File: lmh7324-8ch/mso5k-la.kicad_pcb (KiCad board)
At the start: 4 copper layers, 40 x 44 mm, 101 parts, among them IC201 lmh7324, IC401 lmh7324, J101 out, J102 in, J103 3mm, J104 3mm, J105 3mm, J106 3mm, U401 ATtiny85-20SU

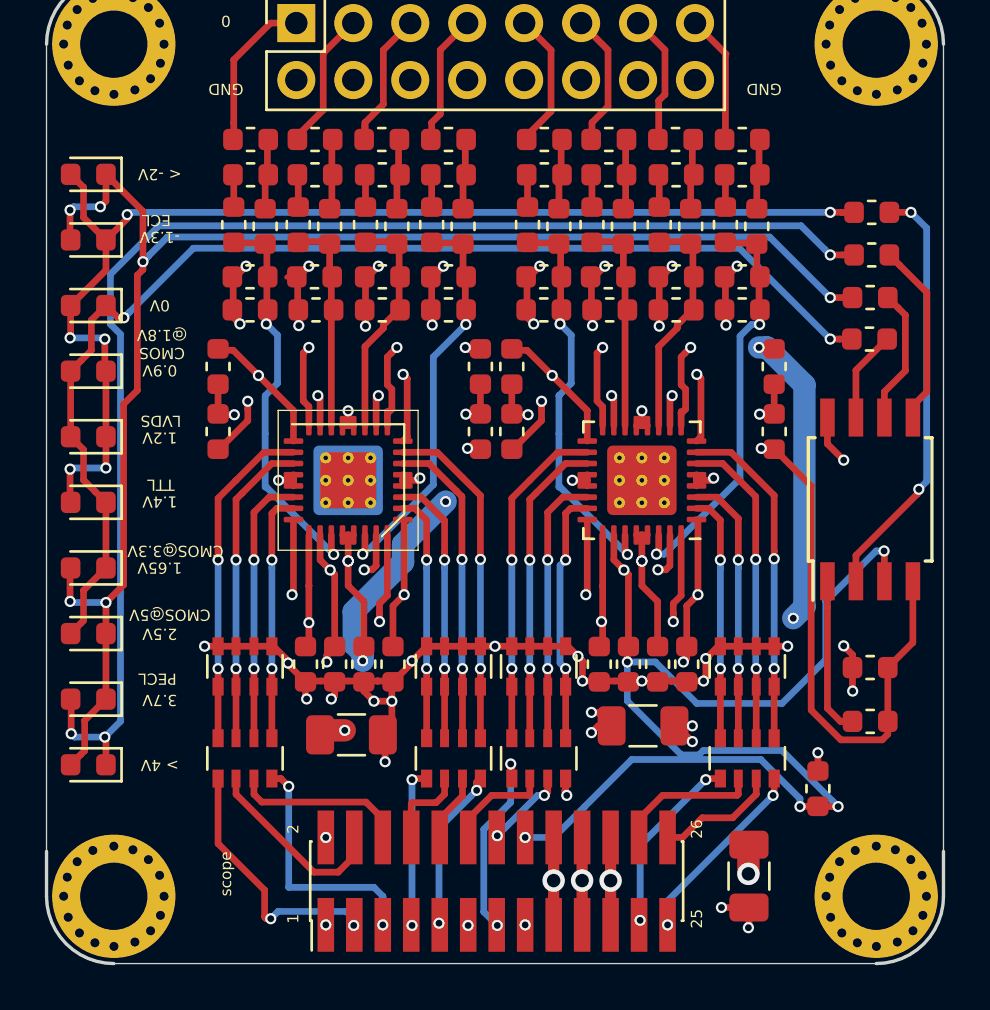
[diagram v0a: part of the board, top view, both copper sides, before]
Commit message: Added breakout
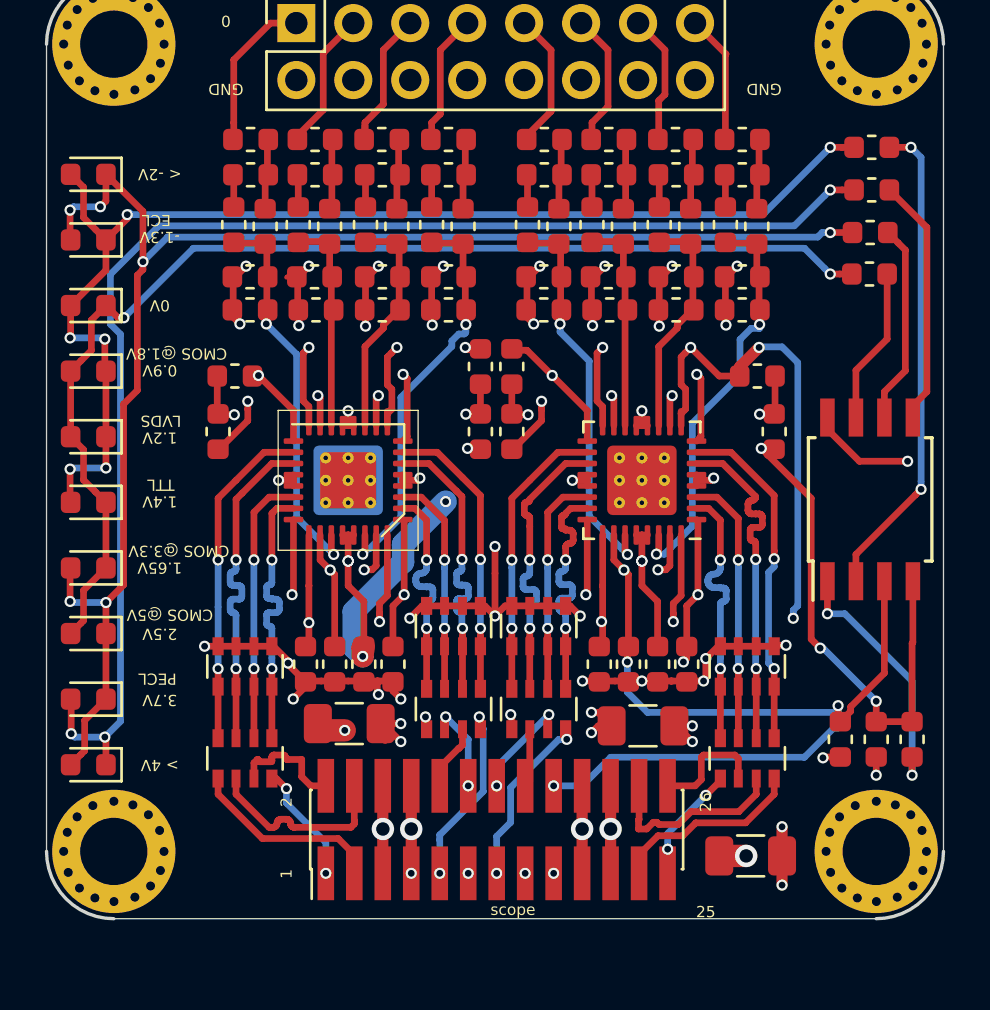
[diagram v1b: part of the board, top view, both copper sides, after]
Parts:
- moved C417 3.21 mm to (82.0, 179.0), turned to 90 degrees
- moved R418 2.90 mm to (81.8, 154.5)
- moved R419 2.90 mm to (81.7, 156.4)
- moved R420 2.90 mm to (81.7, 158.2)
- moved R421 2.90 mm to (81.8, 152.6)
- moved C104 2.42 mm to (80.4, 179.0), turned to 270 degrees
- moved J101 2.30 mm to (65.1, 183.0)
- moved RN202 2.20 mm to (67.0, 177.7)
- moved RN404 2.20 mm to (63.1, 177.7)
- moved R417 2.03 mm to (83.6, 179.0), turned to 90 degrees
- moved J104 2.00 mm to (48.0, 184.0)
- moved J106 2.00 mm to (82.0, 184.0)
- moved RN201 1.80 mm to (67.0, 173.9)
- moved RN403 1.80 mm to (63.1, 173.9)
- moved C102 0.90 mm to (76.4, 184.2), turned to 0 degrees
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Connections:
- J101 pad 1: GND -> D0-
- J101 pad 11: D4- -> D3-
- J101 pad 12: D5+ -> D3+
- J101 pad 13: D5- -> D4-
- J101 pad 15: GND -> D5-
- J101 pad 16: Vref -> D5+
- J101 pad 17: -2V5 -> GND
- J101 pad 18: -2V5 -> Vref
- J101 pad 2: GND -> D0+
- J101 pad 23: D7- -> D6-
- J101 pad 24: D7+ -> D6+
- J101 pad 25: D6- -> D7-
- J101 pad 26: D6+ -> D7+
- J101 pad 5: D0- -> -2V5
- J101 pad 6: D0+ -> -2V5
- J101 pad 7: D3- -> GND
- J101 pad 8: D3+ -> GND
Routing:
- net GND: track 272.3 -> 233.2 mm, vias 43 -> 44
- net Vref: track 144.4 -> 129.9 mm, vias 16 -> 13
- net -2V5: track 127.7 -> 113.6 mm, vias 16 -> 18
- net +2V5: track 155.2 -> 167.3 mm, vias 14 -> 13
- net +4V: track 108.2 -> 100.1 mm
- net D0-: track 12.3 -> 5.41 mm
- net Net-(R417-Pad1): track 7.03 -> 11.5 mm, vias 0 -> 2
- net D7-: track 8.38 -> 5.20 mm
- net D6+: track 5.45 -> 8.61 mm
- net Net-(R420-Pad2): track 4.08 -> 6.98 mm
- net Net-(R419-Pad2): track 6.06 -> 8.96 mm
- net Net-(R418-Pad2): track 8.20 -> 11.1 mm
- net D1-: track 11.9 -> 9.01 mm, vias 2 -> 0
- net Net-(R421-Pad2): track 19.0 -> 21.7 mm
- net D0+: track 7.73 -> 5.31 mm
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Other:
- board size 40 x 44 mm -> 40 x 42 mm
- board text added: "CMOS @3.3V"
- board text added: "CMOS @5V"
- board text removed: "CMOS@3.3V"
- board text removed: "CMOS@5V"

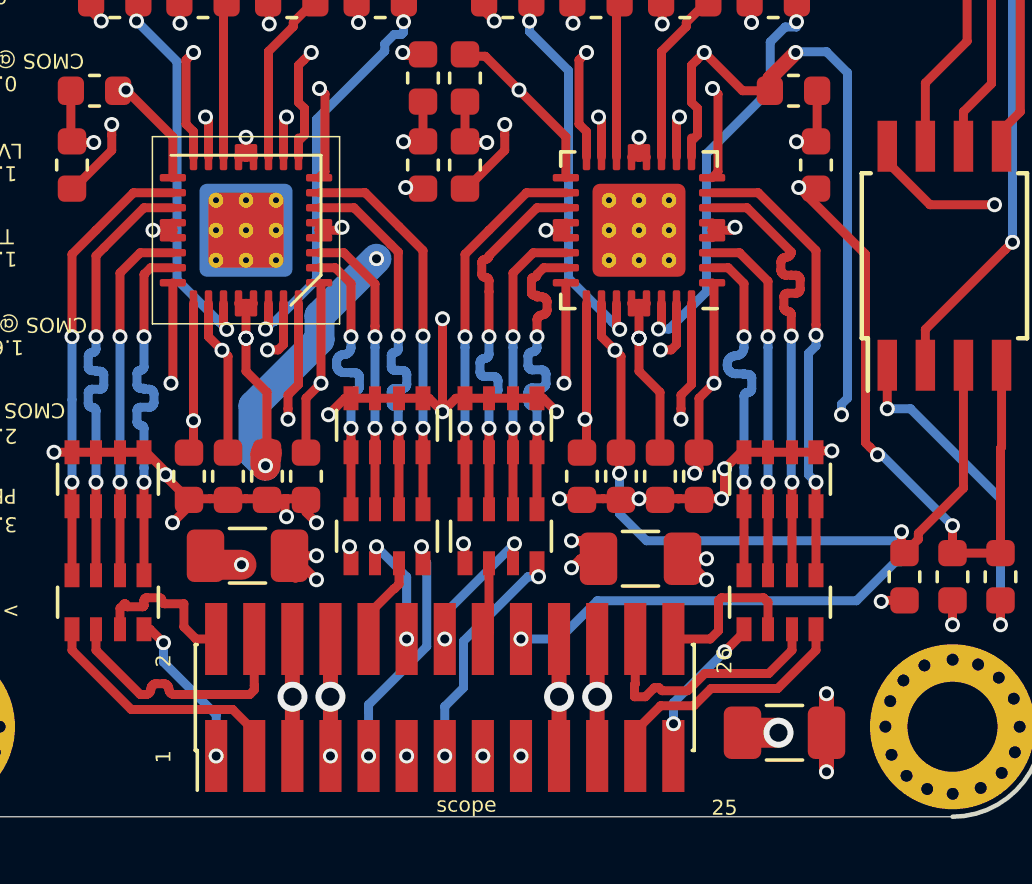
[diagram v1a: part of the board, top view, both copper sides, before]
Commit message: Switched to 0805 on the pod for the large bulk caps
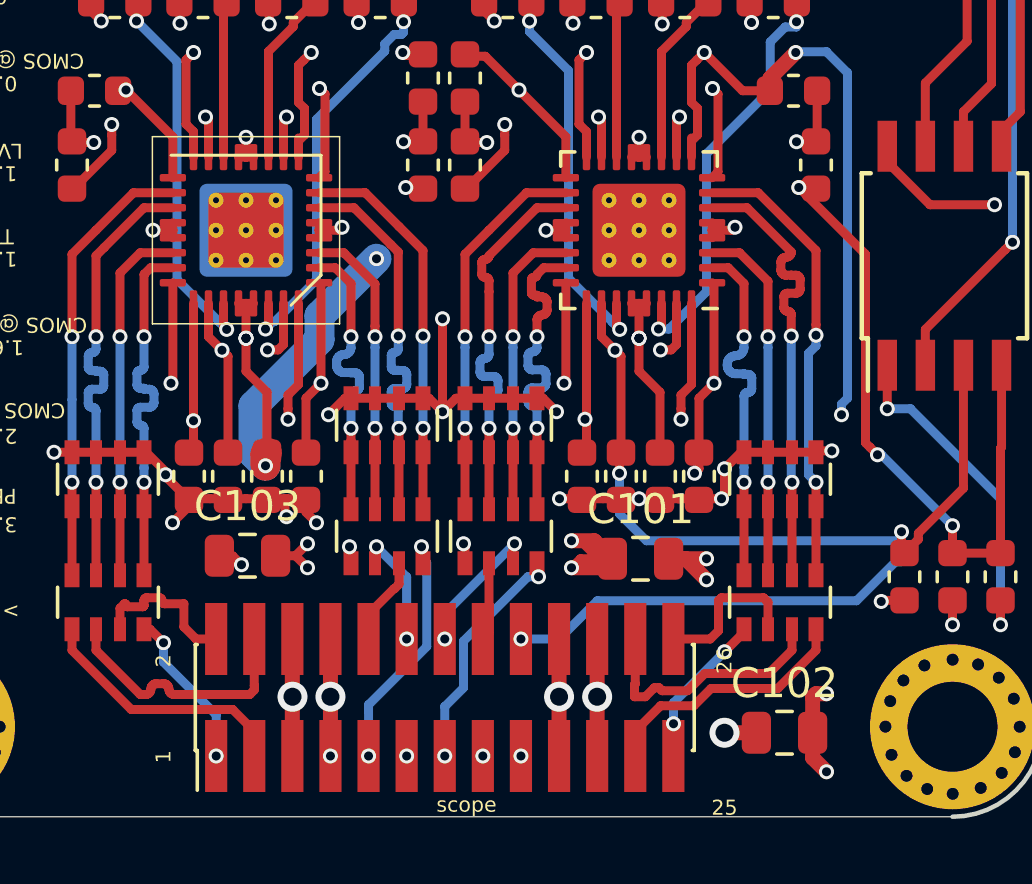
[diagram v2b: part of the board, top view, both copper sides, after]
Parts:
- added G***: LOGO, lmh7324-8ch:qrcode, B.Cu at (65.2, 157.7)
- C101, C102, C103: footprint Capacitor_SMD:C_1206_3216Metric -> Capacitor_SMD:C_0805_2012Metric
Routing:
- net +2V5: track 167.3 -> 163.8 mm
- net +4V: track 100.1 -> 103.2 mm
- net GND: track 233.2 -> 235.0 mm
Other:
- board text added: "MSO5k LMH7324 8 channel LA pod https://dren.dk https://gitlab.com/dren.dk/mso5k-la-pod 2019-01-30"

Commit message: Added proper readme
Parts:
- added C217: 10n, Capacitor_SMD:C_0402_1005Metric, B.Cu at (32.1, 35.6)
- added C218: 10n, Capacitor_SMD:C_0402_1005Metric, B.Cu at (28.6, 39.2)
- added C219: 10n, Capacitor_SMD:C_0402_1005Metric, B.Cu at (29.7, 35.7)
- added C220: 10n, Capacitor_SMD:C_0402_1005Metric, B.Cu at (33.3, 39.3)
- added C221: 10n, Capacitor_SMD:C_0402_1005Metric, B.Cu at (29.6, 40.1)
- added C222: 10n, Capacitor_SMD:C_0402_1005Metric, B.Cu at (33.1, 36.6)
- added C223: 10n, Capacitor_SMD:C_0402_1005Metric, B.Cu at (32.2, 40.1)
- added C224: 10n, Capacitor_SMD:C_0402_1005Metric, B.Cu at (28.7, 36.7)
- added C225: 10n, Capacitor_SMD:C_0402_1005Metric, B.Cu at (33.0, 38.0)
- added C226: 10n, Capacitor_SMD:C_0402_1005Metric, B.Cu at (30.9, 40.0)
- added C227: 10n, Capacitor_SMD:C_0402_1005Metric, B.Cu at (30.9, 35.9)
- added C228: 10n, Capacitor_SMD:C_0402_1005Metric, B.Cu at (28.9, 38.0)
- added C301: 10n, Capacitor_SMD:C_0402_1005Metric, B.Cu at (45.4, 40.0)
- added C302: 10n, Capacitor_SMD:C_0402_1005Metric, B.Cu at (41.7, 36.6)
- added C303: 10n, Capacitor_SMD:C_0402_1005Metric, B.Cu at (42.7, 35.7)
- added C304: 10n, Capacitor_SMD:C_0402_1005Metric, B.Cu at (46.5, 36.6)
- added C305: 10n, Capacitor_SMD:C_0402_1005Metric, B.Cu at (42.7, 40.1)
- added C306: 10n, Capacitor_SMD:C_0402_1005Metric, B.Cu at (41.7, 39.2)
- added C307: 10n, Capacitor_SMD:C_0402_1005Metric, B.Cu at (45.3, 35.7)
- added C308: 10n, Capacitor_SMD:C_0402_1005Metric, B.Cu at (46.5, 39.2)
- added C309: 10n, Capacitor_SMD:C_0402_1005Metric, B.Cu at (46.1, 38.0)
- added C310: 10n, Capacitor_SMD:C_0402_1005Metric, B.Cu at (44.0, 35.9)
- added C311: 10n, Capacitor_SMD:C_0402_1005Metric, B.Cu at (42.0, 38.0)
- added C312: 10n, Capacitor_SMD:C_0402_1005Metric, B.Cu at (44.0, 40.0)
- moved RN402 134.6 mm to (26.3, 48.1)
- moved RN204 134.6 mm to (48.8, 48.1)
- moved RN401 134.2 mm to (26.3, 44.4)
- moved RN203 134.2 mm to (48.8, 44.4)
- moved C101 132.4 mm to (44.1, 48.9)
- moved C102 132.4 mm to (48.9, 54.7)
- moved C103 132.4 mm to (31.0, 48.8)
- moved C104 132.4 mm to (52.9, 49.5)
- moved C201 132.4 mm to (39.0, 26.6)
- moved C202 132.4 mm to (41.8, 26.6)
- moved C203 132.4 mm to (39.7, 30.4)
- moved C204 132.4 mm to (42.6, 30.4)
- moved C205 132.4 mm to (43.5, 46.1)
- moved C206 132.4 mm to (38.2, 35.8)
- moved C207 132.4 mm to (42.1, 46.1)
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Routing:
- net GND: track 235.0 -> 252.5 mm, vias 44 -> 48
- net +4V: track 103.2 -> 86.4 mm, vias 14 -> 19
- net +2V5: track 163.8 -> 155.6 mm, vias 13 -> 22
- net D2+: track 2.96 -> 8.95 mm, vias 0 -> 2
- net D5+: track 2.61 -> 7.98 mm, vias 0 -> 2
- net D0+: track 5.31 -> 10.5 mm, vias 0 -> 2
- net D7+: track 5.27 -> 10.1 mm
- net D3+: track 4.06 -> 8.66 mm
- net -2V5: track 113.7 -> 118.2 mm, vias 18 -> 16
- net D4+: track 4.81 -> 9.00 mm
- net D6-: track 8.67 -> 11.8 mm, vias 0 -> 2
- net D1-: track 9.01 -> 12.0 mm
- net D0-: track 5.41 -> 8.22 mm
- net D7-: track 5.20 -> 7.98 mm, vias 2 -> 0
- net /Ch 0-3/A-: track 12.2 -> 9.59 mm, vias 2 -> 0
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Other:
- board text added: "MSO5k LMH7324 8 channel LA pod https://dren.dk https://gitlab.com/dren.dk/mso5k-la-pod 2019-02-14"
- board text removed: "MSO5k LMH7324 8 channel LA pod https://dren.dk https://gitlab.com/dren.dk/mso5k-la-pod 2019-01-30"

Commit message: Added fixes for E1 and E2
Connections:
- D407 pad 2: Net-(D403-Pad2) -> Net-(D401-Pad1)
- D408 pad 1: Net-(D403-Pad2) -> Net-(D401-Pad1)
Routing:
- net Net-(D401-Pad1): track 60.2 -> 65.5 mm, vias 3 -> 4
- net Net-(D403-Pad2): track 51.8 -> 53.2 mm
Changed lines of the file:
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@@
     (thickness 1.6)
     (drawings 34)
-    (tracks 1692)
+    (tracks 1699)
     (zones 0)
     (modules 126)
@@
     (fp_line (start 0.8 -0.4) (end -0.5 -0.4) (layer F.Fab) (width 0.1))
     (pad 2 smd roundrect (at 0.7875 0 180) (size 0.875 0.95) (layers F.Cu F.Paste F.Mask) (roundrect_rratio 0.25)
-      (net 72 "Net-(D403-Pad2)"))
+      (net 71 "Net-(D401-Pad1)"))
     (pad 1 smd roundrect (at -0.7875 0 180) (size 0.875 0.95) (layers F.Cu F.Paste F.Mask) (roundrect_rratio 0.25)
       (net 73 "Net-(D405-Pad2)"))
@@
     )
     (pad 1 smd roundrect (at -0.7875 0 180) (size 0.875 0.95) (layers F.Cu F.Paste F.Mask) (roundrect_rratio 0.25)
-      (net 72 "Net-(D403-Pad2)"))
+      (net 71 "Net-(D401-Pad1)"))
     (pad 2 smd roundrect (at 0.7875 0 180) (size 0.875 0.95) (layers F.Cu F.Paste F.Mask) (roundrect_rratio 0.25)
       (net 73 "Net-(D405-Pad2)"))
@@
   (segment (start 33.125 32.025) (end 36.175 32.025) (width 1) (layer 3_Misc) (net 1))
   (segment (start 36.175 32.025) (end 37.575 32.025) (width 1) (layer 3_Misc) (net 1))
-  (via (at 41.8 48.3) (size 0.5) (drill 0.3) (layers F.Cu B.Cu) (net 1) (status 1000000))
+  (via (at 41.8 48.3) (size 0.5) (drill 0.3) (layers F.Cu B.Cu) (net 1))
   (via (at 42.655 53.5) (size 1) (drill 0.6) (layers F.Cu B.Cu) (net 1))
   (segment (start 41.8 48.3) (end 42.1 48.3) (width 0.3) (layer F.Cu) (net 1) (status 20))
@@
   (segment (start 18.55 41.881928) (end 18.574213 41.857715) (width 0.3) (layer F.Cu) (net 70) (status 30))
   (segment (start 18.55 43.35) (end 18.55 41.881928) (width 0.3) (layer F.Cu) (net 70) (status 20))
-  (segment (start 20.15 43.4) (end 20.936723 42.613277) (width 0.3) (layer F.Cu) (net 70))
   (segment (start 18.7 25.75) (end 18.55 25.9) (width 0.3) (layer B.Cu) (net 70))
   (segment (start 19.9 25.75) (end 18.7 25.75) (width 0.3) (layer B.Cu) (net 70))
   (via (at 21.8 28.2) (size 0.5) (drill 0.3) (layers F.Cu B.Cu) (net 70))
-  (segment (start 21.8 28.553553) (end 21.55 28.803553) (width 0.3) (layer F.Cu) (net 70))
-  (segment (start 21.8 28.2) (end 21.8 28.553553) (width 0.3) (layer F.Cu) (net 70))
-  (segment (start 21.55 33.936723) (end 20.936723 34.55) (width 0.3) (layer F.Cu) (net 70))
-  (segment (start 21.55 28.803553) (end 21.55 33.936723) (width 0.3) (layer F.Cu) (net 70))
-  (segment (start 20.936723 42.613277) (end 20.936723 34.55) (width 0.3) (layer F.Cu) (net 70))
   (segment (start 21.8 25.954968) (end 20.149213 24.304181) (width 0.3) (layer F.Cu) (net 70) (status 20))
   (segment (start 21.8 28.2) (end 21.8 25.954968) (width 0.3) (layer F.Cu) (net 70))
@@
   (segment (start 21.8 28.2) (end 22.898227 27.101773) (width 0.3) (layer B.Cu) (net 70))
   (segment (start 22.898227 27.101773) (end 51.894674 27.101773) (width 0.3) (layer B.Cu) (net 70))
+  (segment (start 22.090002 41.459998) (end 22.090002 28.490002) (width 0.3) (layer F.Cu) (net 70))
+  (segment (start 20.15 43.4) (end 22.090002 41.459998) (width 0.3) (layer F.Cu) (net 70))
+  (segment (start 22.049999 28.449999) (end 21.8 28.2) (width 0.3) (layer F.Cu) (net 70))
+  (segment (start 22.090002 28.490002) (end 22.049999 28.449999) (width 0.3) (layer F.Cu) (net 70))
   (segment (start 53.5125 25) (end 52.975 25) (width 0.3) (layer F.Cu) (net 71) (status 10))
   (via (at 52.45 25) (size 0.5) (drill 0.3) (layers F.Cu B.Cu) (net 71))
@@
   (segment (start 22.510234 26.601762) (end 50.848238 26.601762) (width 0.3) (layer B.Cu) (net 71))
   (segment (start 20.799989 48.700011) (end 20.799989 31.438001) (width 0.3) (layer B.Cu) (net 71))
-  (segment (start 20.349989 30.988001) (end 20.349989 28.762007) (width 0.3) (layer B.Cu) (net 71))
   (segment (start 20.799989 31.438001) (end 20.349989 30.988001) (width 0.3) (layer B.Cu) (net 71))
   (segment (start 20.1 49.4) (end 20.799989 48.700011) (width 0.3) (layer B.Cu) (net 71))
+  (segment (start 19.035825 32.619336) (end 19.035825 32.194175) (width 0.3) (layer F.Cu) (net 71))
+  (segment (start 18.574213 33.080948) (end 19.035825 32.619336) (width 0.3) (layer F.Cu) (net 71))
+  (segment (start 19.035825 32.194175) (end 19.4 31.83) (width 0.3) (layer F.Cu) (net 71))
+  (segment (start 19.4 30.904572) (end 20.149213 30.155359) (width 0.3) (layer F.Cu) (net 71))
+  (segment (start 19.4 31.83) (end 19.4 30.904572) (width 0.3) (layer F.Cu) (net 71))
+  (via (at 20.72 29.05) (size 0.5) (drill 0.3) (layers F.Cu B.Cu) (net 71))
+  (segment (start 20.149213 30.155359) (end 20.149213 29.620787) (width 0.3) (layer F.Cu) (net 71))
+  (segment (start 20.149213 29.620787) (end 20.72 29.05) (width 0.3) (layer F.Cu) (net 71))
+  (segment (start 20.366447 29.05) (end 20.349989 29.066458) (width 0.3) (layer B.Cu) (net 71))
+  (segment (start 20.72 29.05) (end 20.366447 29.05) (width 0.3) (layer B.Cu) (net 71))
+  (segment (start 20.349989 30.988001) (end 20.349989 29.07) (width 0.3) (layer B.Cu) (net 71))
+  (segment (start 20.349989 29.066458) (end 20.349989 29.07) (width 0.3) (layer B.Cu) (net 71))
+  (segment (start 20.349989 29.07) (end 20.349989 28.762007) (width 0.3) (layer B.Cu) (net 71))
   (segment (start 53.4125 28.75) (end 52.875 28.75) (width 0.3) (layer F.Cu) (net 72) (status 10))
   (via (at 52.45 28.75) (size 0.5) (drill 0.3) (layers F.Cu B.Cu) (net 72))
   (segment (start 52.875 28.75) (end 52.45 28.75) (width 0.3) (layer F.Cu) (net 72))
-  (segment (start 18.574213 33.080948) (end 18.574213 36.006537) (width 0.3) (layer F.Cu) (net 72) (status 30))
   (segment (start 20.149213 38.932126) (end 20.149213 41.857715) (width 0.3) (layer F.Cu) (net 72) (status 30))
-  (segment (start 19.499999 32.155162) (end 19.035825 32.619336) (width 0.3) (layer F.Cu) (net 72))
-  (segment (start 19.035825 32.619336) (end 18.574213 33.080948) (width 0.3) (layer F.Cu) (net 72) (status 20))
-  (segment (start 19.499999 30.804573) (end 19.499999 32.155162) (width 0.3) (layer F.Cu) (net 72))
-  (segment (start 20.149213 30.155359) (end 19.499999 30.804573) (width 0.3) (layer F.Cu) (net 72) (status 10))
   (segment (start 19.687601 38.470514) (end 20.149213 38.932126) (width 0.3) (layer F.Cu) (net 72) (status 20))
   (segment (start 18.574213 36.006537) (end 19.150001 36.582325) (width 0.3) (layer F.Cu) (net 72) (status 10))
@@
   (segment (start 20.149213 41.857715) (end 19.150001 42.856927) (width 0.3) (layer F.Cu) (net 72) (status 10))
   (segment (start 19.035825 44.321692) (end 18.574213 44.783304) (width 0.3) (layer F.Cu) (net 72) (status 20))
-  (segment (start 20.149213 30.155359) (end 20.693854 30.7) (width 0.3) (layer F.Cu) (net 72) (status 10))
-  (segment (start 20.693854 30.7) (end 20.94999 30.7) (width 0.3) (layer F.Cu) (net 72))
-  (via (at 20.94999 30.7) (size 0.5) (drill 0.3) (layers F.Cu B.Cu) (net 72))
   (segment (start 51.301782 27.601782) (end 52.200001 28.500001) (width 0.3) (layer B.Cu) (net 72))
   (segment (start 52.200001 28.500001) (end 52.45 28.75) (width 0.3) (layer B.Cu) (net 72))
-  (segment (start 20.94999 30.7) (end 24.048208 27.601782) (width 0.3) (layer B.Cu) (net 72))
   (segment (start 24.048208 27.601782) (end 51.301782 27.601782) (width 0.3) (layer B.Cu) (net 72))
+  (segment (start 20.686713 38.932126) (end 21.49 38.128839) (width 0.3) (layer F.Cu) (net 72))
+  (segment (start 20.149213 38.932126) (end 20.686713 38.932126) (width 0.3) (layer F.Cu) (net 72))
+  (segment (start 21.49 38.128839) (end 21.49 37.02) (width 0.3) (layer F.Cu) (net 72))
+  (via (at 21.49 37.02) (size 0.5) (drill 0.3) (layers F.Cu B.Cu) (net 72))
+  (segment (start 21.49 30.15999) (end 24.048208 27.601782) (width 0.3) (layer B.Cu) (net 72))
+  (segment (start 21.49 37.02) (end 21.49 30.15999) (width 0.3) (layer B.Cu) (net 72))
   (segment (start 53.5125 23.1) (end 52.975 23.1) (width 0.3) (layer F.Cu) (net 73) (status 10))
   (via (at 52.45 23.1) (size 0.5) (drill 0.3) (layers F.Cu B.Cu) (net 73))
